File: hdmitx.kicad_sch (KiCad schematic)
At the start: 69 parts, among them J4 HDMI_CONN, U3 IT6613, U8 PCM1862, Y2 24.576MHz

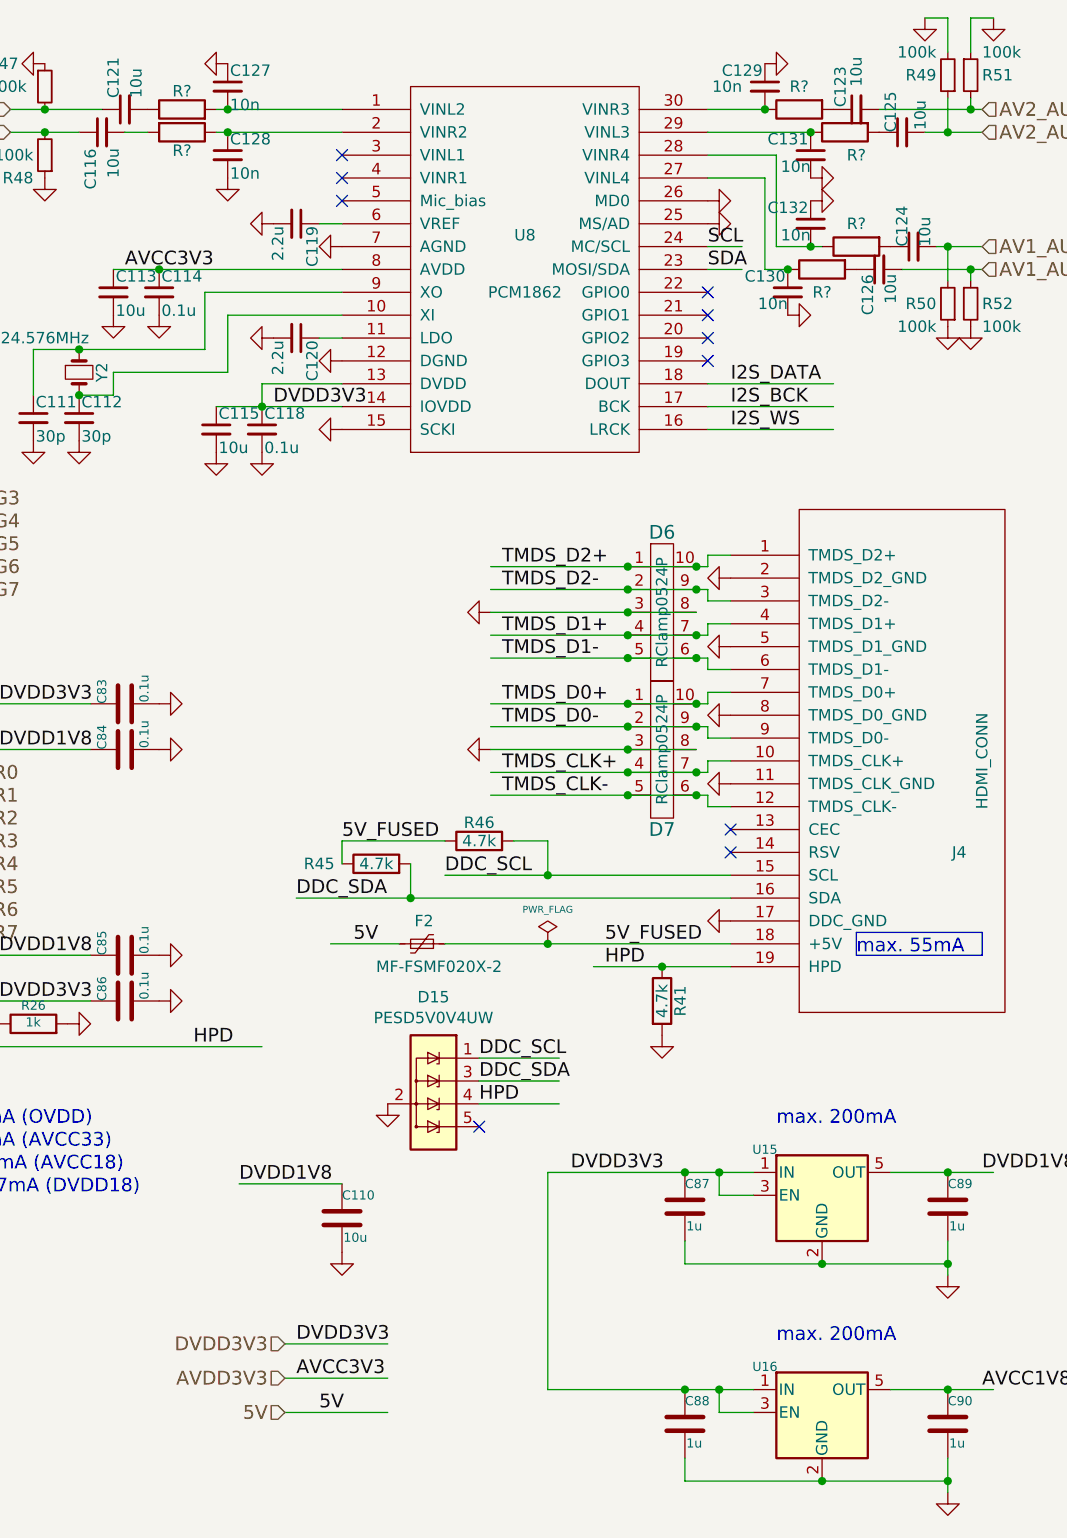
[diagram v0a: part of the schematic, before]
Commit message: additional updates for PCB v1.8
* change to 4-layer stackup for better power delivery
* choose another FPGA pin for PCB version indicator
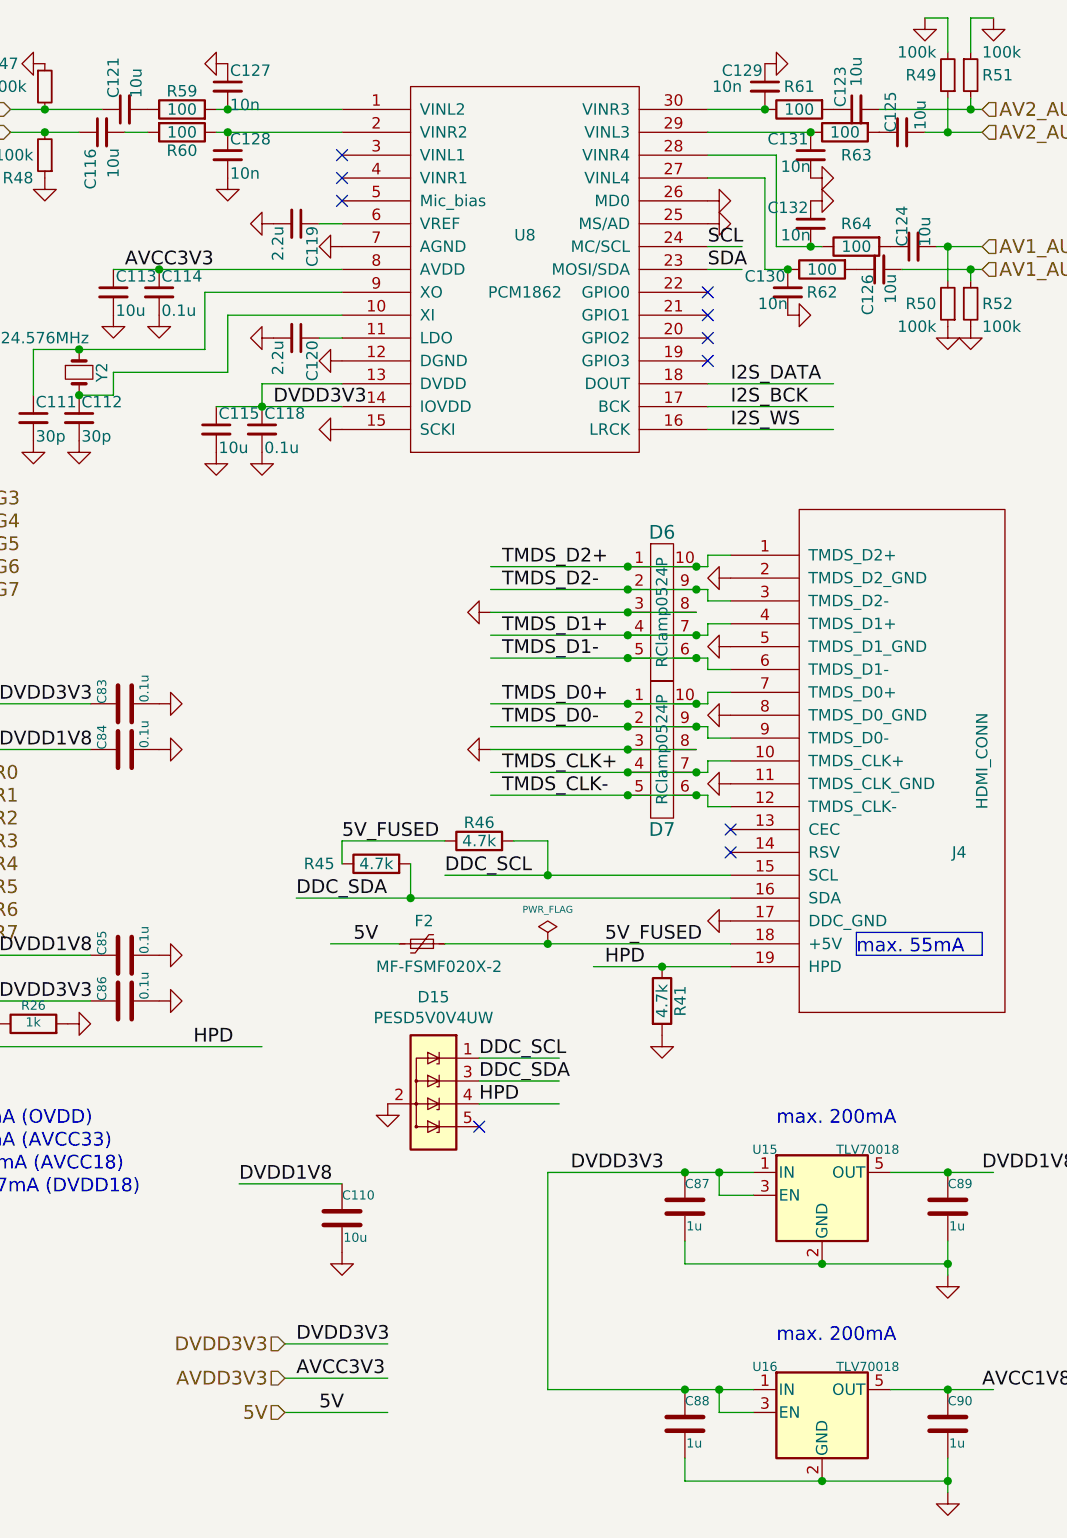
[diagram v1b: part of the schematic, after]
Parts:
- R59, R60, R61, R62, R63, R64: renamed from R?; value (none) -> 100; footprint (none) -> custom_components:SM0603_Resistor_libcms
- U15, U16: value (none) -> TLV70018; footprint (none) -> custom_components:SOT-23-5_Handsoldering
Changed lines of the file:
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@@
       (effects (font (size 1.016 1.016)))
     )
-    (property "Value" "" (id 1) (at 257.81 138.43 0)
+    (property "Value" "TLV70018" (id 1) (at 257.81 138.43 0)
       (effects (font (size 1.016 1.016)))
     )
-    (property "Footprint" "" (id 2) (at 252.73 140.97 0)
+    (property "Footprint" "custom_components:SOT-23-5_Handsoldering" (id 2) (at 252.73 140.97 0)
       (effects (font (size 0.889 0.889) italic) hide)
     )
@@
       (effects (font (size 1.016 1.016)))
     )
-    (property "Value" "" (id 1) (at 257.81 162.56 0)
+    (property "Value" "TLV70018" (id 1) (at 257.81 162.56 0)
       (effects (font (size 1.016 1.016)))
     )
-    (property "Footprint" "" (id 2) (at 252.73 165.1 0)
+    (property "Footprint" "custom_components:SOT-23-5_Handsoldering" (id 2) (at 252.73 165.1 0)
       (effects (font (size 0.889 0.889) italic) hide)
     )
@@
   (symbol (lib_id "Device:R") (at 181.61 22.86 90) (unit 1)
     (in_bom yes) (on_board yes)
-    (property "Reference" "R?" (id 0) (at 181.61 20.828 90))
-    (property "Value" "" (id 1) (at 181.61 22.86 90))
-    (property "Footprint" "" (id 2) (at 181.61 24.638 90)
+    (property "Reference" "R59" (id 0) (at 181.61 20.828 90))
+    (property "Value" "100" (id 1) (at 181.61 22.86 90))
+    (property "Footprint" "custom_components:SM0603_Resistor_libcms" (id 2) (at 181.61 24.638 90)
       (effects (font (size 0.762 0.762)) hide)
     )
@@
   (symbol (lib_id "Device:R") (at 181.61 25.4 270) (unit 1)
     (in_bom yes) (on_board yes)
-    (property "Reference" "R?" (id 0) (at 181.61 27.432 90))
-    (property "Value" "" (id 1) (at 181.61 25.4 90))
-    (property "Footprint" "" (id 2) (at 181.61 23.622 90)
+    (property "Reference" "R60" (id 0) (at 181.61 27.432 90))
+    (property "Value" "100" (id 1) (at 181.61 25.4 90))
+    (property "Footprint" "custom_components:SM0603_Resistor_libcms" (id 2) (at 181.61 23.622 90)
       (effects (font (size 0.762 0.762)) hide)
     )
@@
   (symbol (lib_id "Device:R") (at 250.19 22.86 90) (mirror x) (unit 1)
     (in_bom yes) (on_board yes)
-    (property "Reference" "R?" (id 0) (at 250.19 20.32 90))
-    (property "Value" "" (id 1) (at 250.19 22.86 90))
-    (property "Footprint" "" (id 2) (at 250.19 21.082 90)
+    (property "Reference" "R61" (id 0) (at 250.19 20.32 90))
+    (property "Value" "100" (id 1) (at 250.19 22.86 90))
+    (property "Footprint" "custom_components:SM0603_Resistor_libcms" (id 2) (at 250.19 21.082 90)
       (effects (font (size 0.762 0.762)) hide)
     )
@@
   (symbol (lib_id "Device:R") (at 255.27 25.4 90) (mirror x) (unit 1)
     (in_bom yes) (on_board yes)
-    (property "Reference" "R?" (id 0) (at 256.54 27.94 90))
-    (property "Value" "" (id 1) (at 255.27 25.4 90))
-    (property "Footprint" "" (id 2) (at 255.27 23.622 90)
+    (property "Reference" "R63" (id 0) (at 256.54 27.94 90))
+    (property "Value" "100" (id 1) (at 255.27 25.4 90))
+    (property "Footprint" "custom_components:SM0603_Resistor_libcms" (id 2) (at 255.27 23.622 90)
       (effects (font (size 0.762 0.762)) hide)
     )
@@
   (symbol (lib_id "Device:R") (at 252.73 40.64 90) (mirror x) (unit 1)
     (in_bom yes) (on_board yes)
-    (property "Reference" "R?" (id 0) (at 252.73 43.18 90))
-    (property "Value" "" (id 1) (at 252.73 40.64 90))
-    (property "Footprint" "" (id 2) (at 252.73 38.862 90)
+    (property "Reference" "R62" (id 0) (at 252.73 43.18 90))
+    (property "Value" "100" (id 1) (at 252.73 40.64 90))
+    (property "Footprint" "custom_components:SM0603_Resistor_libcms" (id 2) (at 252.73 38.862 90)
       (effects (font (size 0.762 0.762)) hide)
     )
@@
   (symbol (lib_id "Device:R") (at 256.54 38.1 90) (mirror x) (unit 1)
     (in_bom yes) (on_board yes)
-    (property "Reference" "R?" (id 0) (at 256.54 35.56 90))
-    (property "Value" "" (id 1) (at 256.54 38.1 90))
-    (property "Footprint" "" (id 2) (at 256.54 36.322 90)
-      (effects (font (size 0.762 0.762)) hide)
-    )
+    (property "Reference" "R64" (id 0) (at 256.54 35.56 90))
+    (property "Value" "100" (id 1) (at 256.54 38.1 90))
+    (property "Footprint" "custom_components:SM0603_Resistor_libcms" (id 2) (at 256.54 36.322 90)
+      (effects (font (size 0.762 0.762)) hide)
+    )
